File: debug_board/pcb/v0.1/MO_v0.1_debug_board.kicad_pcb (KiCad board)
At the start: 2 copper layers, 98.1 x 88 mm, 52 parts, among them j1 DAC_PWR, j10 nRF_PWR, j11 U0_TX, j12 nRF_VBUS, j13 SWDIO, j14 SWDCLK, j15 U0_RX, j16 nRF_DCCH, j2 SD_nFLAG, j3 DAC_nFLAG, j4 nRF_RESET, j5 FW_PWR_FAULT, j6 SD_PWR, j7 3v3_PI, j8 3v3_LDO, j9 GND

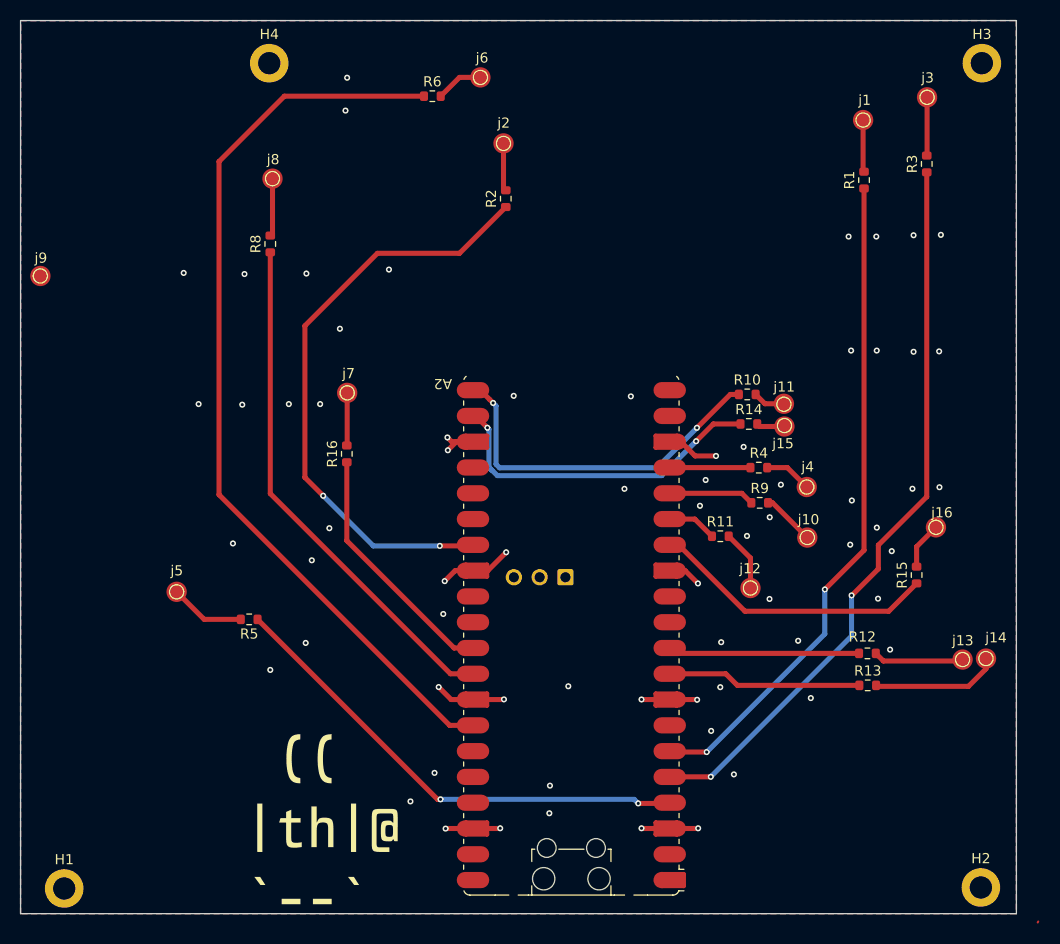
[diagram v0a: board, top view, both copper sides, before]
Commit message: Update debug board to use pi zero instead of pico
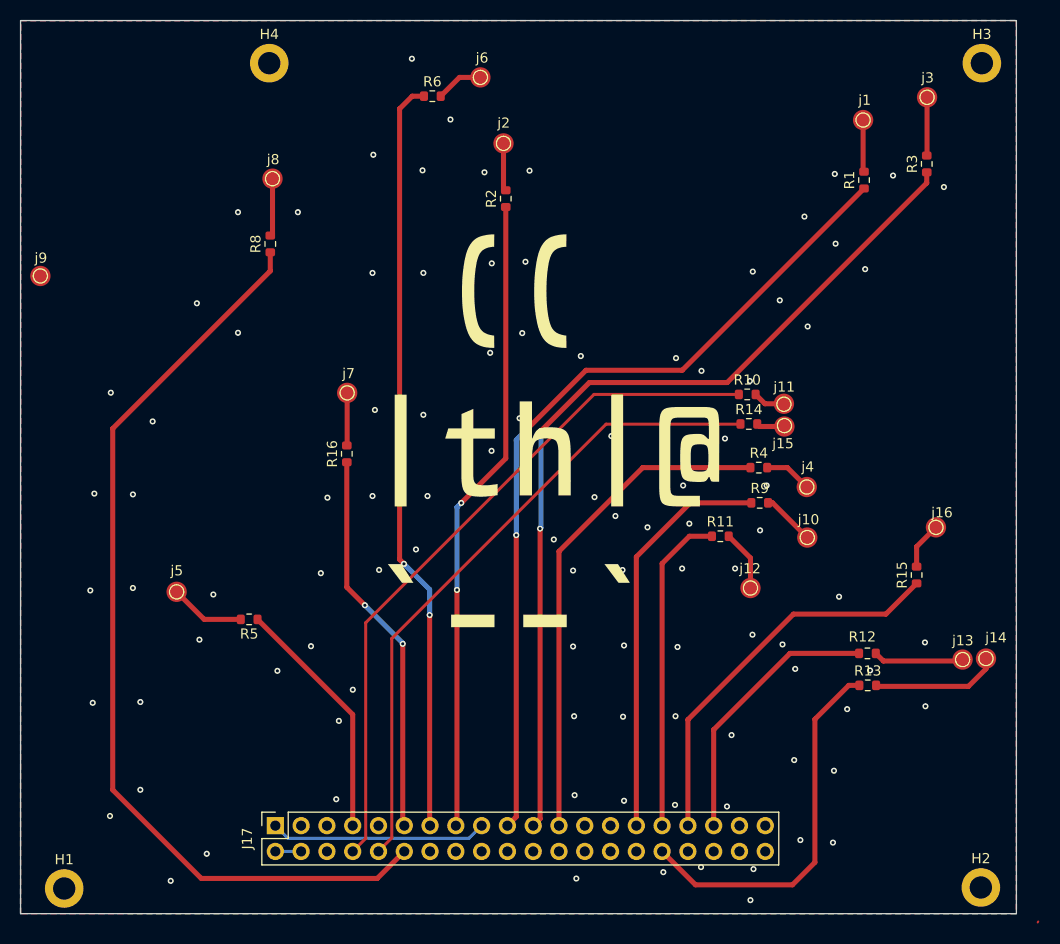
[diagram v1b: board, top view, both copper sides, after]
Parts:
- removed A2: RaspberryPi_Pico_W, Module:RaspberryPi_Pico_W_SMD_HandSolder
- added J17: Raspberry_Pi_4, Connector_PinSocket_2.54mm:PinSocket_2x20_P2.54mm_Vertical, F.Cu at (161.2, 109.6)
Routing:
- net GND: track 44.6 -> 0.00 mm, vias 68 -> 101
- net /3v3_LDO: track 51.1 -> 92.8 mm
- net /nRF_RESET: track 7.95 -> 49.3 mm
- net /U0_TX: track 35.7 -> 69.1 mm, vias 2 -> 0
- net /nRF_PWR: track 8.43 -> 40.0 mm
- net /U0_RX: track 33.4 -> 64.6 mm, vias 2 -> 0
- net /nRF_VBUS: track 4.86 -> 31.8 mm
- net /FW_PWR_FAULT: track 48.1 -> 24.2 mm, vias 2 -> 0
- net Net-(J17-3V3-Pad1): track 0.00 -> 21.3 mm
- net /SWDCLK: track 19.2 -> 37.2 mm
- net /DAC_PWR: track 65.6 -> 82.9 mm
- net /DAC_nFLAG: track 72.4 -> 88.4 mm
- net /SD_PWR: track 90.1 -> 74.8 mm, vias 0 -> 2
- net /3v3_PI: track 24.5 -> 38.1 mm, vias 0 -> 2
- net /nRF_DCCH: track 28.2 -> 38.5 mm
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
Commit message: Clean up silkscreen and fab files for debug board
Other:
- board text added: "TH-1-MO Debug board Rev: 1 31/08/2026 For MO rev: 0 (devkit)"
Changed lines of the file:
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@@
 		(capping no)
 		(filling no)
-		(zone_defaults)
+		(aux_axis_origin 136.08 118.27)
+		(grid_origin 136.08 118.27)
 		(pcbplotparams
 			(layerselection 0x00000000_00000000_55555555_5755f5ff)
@@
 			(usegerberattributes yes)
 			(usegerberadvancedattributes yes)
-			(creategerberjobfile yes)
+			(creategerberjobfile no)
 			(dashed_line_dash_ratio 12)
 			(dashed_line_gap_ratio 3)
@@
 			(plotframeref no)
 			(mode 1)
-			(useauxorigin no)
+			(useauxorigin yes)
 			(pdf_front_fp_property_popups yes)
 			(pdf_back_fp_property_popups yes)
@@
 			(plotpadnumbers no)
 			(hidednponfab no)
-			(sketchdnponfab yes)
-			(crossoutdnponfab yes)
+			(sketchdnponfab no)
+			(crossoutdnponfab no)
 			(subtractmaskfromsilk no)
 			(outputformat 1)
 			(mirror no)
-			(drillshape 1)
+			(drillshape 0)
 			(scaleselection 1)
-			(outputdirectory "")
+			(outputdirectory "fabrication/")
 		)
 	)
@@
 		(layer "Edge.Cuts")
 	)
+	(gr_text "TH-1-MO Debug board\nRev: 1\n31/08/2026\nFor MO rev: 0 (devkit)"
+		(at 188.79 41.75 0)
+		(layer "F.SilkS")
+		(effects
+			(font
+				(size 1.5 1.5)
+				(thickness 0.3)
+				(bold yes)
+			)
+			(justify left bottom)
+		)
+	)
 	(gr_text "DIO"
 		(at 227.13 93.14 90)
@@
 	)
 	(segment
-		(start 219.17 46.83)
-		(end 201.26 64.74)
-		(width 0.5)
-		(layer "F.Cu")
-		(net "/DAC_PWR")
-	)
-	(segment
-		(start 184.91 80.98)
-		(end 184.91 108.73)
-		(width 0.5)
-		(layer "F.Cu")
-		(net "/DAC_PWR")
-	)
-	(segment
-		(start 191.78 64.74)
-		(end 185.96 70.56)
-		(width 0.5)
-		(layer "F.Cu")
-		(net "/DAC_PWR")
-	)
-	(segment
-		(start 184.91 108.73)
-		(end 184.04 109.6)
+		(start 211.62 74.33)
+		(end 213.53 76.24)
 		(width 0.5)
 		(layer "F.Cu")
-		(net "/DAC_PWR")
+		(net "Net-(R4-Pad2)")
 	)
 	(segment
-		(start 201.26 64.74)
-		(end 191.78 64.74)
+		(start 209.63 74.33)
+		(end 211.62 74.33)
 		(width 0.5)
 		(layer "F.Cu")
-		(net "/DAC_PWR")
-	)
-	(via
-		(at 184.91 80.98)
-		(size 0.6)
-		(drill 0.3)
-		(layers "F.Cu" "B.Cu")
-		(net "/DAC_PWR")
-	)
-	(via
-		(at 185.96 70.56)
-		(size 0.6)
-		(drill 0.3)
-		(layers "F.Cu" "B.Cu")
-		(net "/DAC_PWR")
+		(net "Net-(R4-Pad2)")
 	)
 	(segment
-		(start 184.91 71.61)
-		(end 184.91 80.98)
-		(width 0.5)
+		(start 161.18 109.6)
+		(end 162.42 110.84)
+		(width 0.3)
 		(layer "B.Cu")
-		(net "/DAC_PWR")
+		(net "Net-(J17-3V3-Pad1)")
 	)
 	(segment
-		(start 185.96 70.56)
-		(end 184.91 71.61)
-		(width 0.5)
+		(start 180.26 110.84)
+		(end 181.5 109.6)
+		(width 0.3)
 		(layer "B.Cu")
-		(net "/DAC_PWR")
-	)
-	(segment
-		(start 204.36 100.15)
-		(end 204.36 109.6)
-		(width 0.5)
-		(layer "F.Cu")
-		(net "/SWDIO")
-	)
-	(segment
-		(start 218.68 92.63)
-		(end 211.88 92.63)
-		(width 0.5)
-		(layer "F.Cu")
-		(net "/SWDIO")
-	)
-	(segment
-		(start 211.88 92.63)
-		(end 204.36 100.15)
-		(width 0.5)
-		(layer "F.Cu")
-		(net "/SWDIO")
-	)
-	(segment
-		(start 212.22 88.76)
-		(end 201.82 99.16)
-		(width 0.5)
-		(layer "F.Cu")
-		(net "/nRF_DCCH")
-	)
-	(segment
-		(start 201.82 99.16)
-		(end 201.82 109.6)
-		(width 0.5)
-		(layer "F.Cu")
-		(net "/nRF_DCCH")
-	)
-	(segment
-		(start 221.325 88.76)
-		(end 212.22 88.76)
-		(width 0.5)
-		(layer "F.Cu")
-		(net "/nRF_DCCH")
-	)
-	(segment
-		(start 224.35 85.735)
-		(end 221.325 88.76)
-		(width 0.5)
-		(layer "F.Cu")
-		(net "/nRF_DCCH")
-	)
-	(segment
-		(start 189.12 82.58)
-		(end 189.12 109.6)
-		(width 0.5)
-		(layer "F.Cu")
-		(net "/nRF_RESET")
+		(net "Net-(J17-3V3-Pad1)")
 	)
 	(segment
-		(start 207.98 74.33)
-		(end 197.37 74.33)
-		(width 0.5)
-		(layer "F.Cu")
-		(net "/nRF_RESET")
+		(start 162.42 110.84)
+		(end 180.26 110.84)
+		(width 0.3)
+		(layer "B.Cu")
+		(net "Net-(J17-3V3-Pad1)")
 	)
 	(segment
-		(start 197.37 74.33)
-		(end 189.12 82.58)
-		(width 0.5)
-		(layer "F.Cu")
-		(net "/nRF_RESET")
+		(start 163.72 112.14)
+		(end 161.18 112.14)
+		(width 0.3)
+		(layer "B.Cu")
+		(net "Net-(J17-5V-Pad2)")
 	)
 	(segment
@@
 	)
 	(segment
-		(start 211.62 74.33)
-		(end 213.53 76.24)
+		(start 219.17 46.83)
+		(end 201.26 64.74)
 		(width 0.5)
 		(layer "F.Cu")
-		(net "Net-(R4-Pad2)")
+		(net "/DAC_PWR")
 	)
 	(segment
-		(start 209.63 74.33)
-		(end 211.62 74.33)
+		(start 184.91 80.98)
+		(end 184.91 108.73)
 		(width 0.5)
 		(layer "F.Cu")
-		(net "Net-(R4-Pad2)")
+		(net "/DAC_PWR")
+	)
+	(segment
+		(start 191.78 64.74)
+		(end 185.96 70.56)
+		(width 0.5)
+		(layer "F.Cu")
+		(net "/DAC_PWR")
+	)
+	(segment
+		(start 184.91 108.73)
+		(end 184.04 109.6)
+		(width 0.5)
+		(layer "F.Cu")
+		(net "/DAC_PWR")
+	)
+	(segment
+		(start 201.26 64.74)
+		(end 191.78 64.74)
+		(width 0.5)
+		(layer "F.Cu")
+		(net "/DAC_PWR")
+	)
+	(via
+		(at 184.91 80.98)
+		(size 0.6)
+		(drill 0.3)
+		(layers "F.Cu" "B.Cu")
+		(net "/DAC_PWR")
+	)
+	(via
+		(at 185.96 70.56)
+		(size 0.6)
+		(drill 0.3)
+		(layers "F.Cu" "B.Cu")
+		(net "/DAC_PWR")
+	)
+	(segment
+		(start 184.91 71.61)
+		(end 184.91 80.98)
+		(width 0.5)
+		(layer "B.Cu")
+		(net "/DAC_PWR")
+	)
+	(segment
+		(start 185.96 70.56)
+		(end 184.91 71.61)
+		(width 0.5)
+		(layer "B.Cu")
+		(net "/DAC_PWR")
+	)
+	(segment
+		(start 189.12 82.58)
+		(end 189.12 109.6)
+		(width 0.5)
+		(layer "F.Cu")
+		(net "/nRF_RESET")
+	)
+	(segment
+		(start 207.98 74.33)
+		(end 197.37 74.33)
+		(width 0.5)
+		(layer "F.Cu")
+		(net "/nRF_RESET")
+	)
+	(segment
+		(start 197.37 74.33)
+		(end 189.12 82.58)
+		(width 0.5)
+		(layer "F.Cu")
+		(net "/nRF_RESET")
+	)
+	(segment
+		(start 212.22 88.76)
+		(end 201.82 99.16)
+		(width 0.5)
+		(layer "F.Cu")
+		(net "/nRF_DCCH")
+	)
+	(segment
+		(start 201.82 99.16)
+		(end 201.82 109.6)
+		(width 0.5)
+		(layer "F.Cu")
+		(net "/nRF_DCCH")
+	)
+	(segment
+		(start 221.325 88.76)
+		(end 212.22 88.76)
+		(width 0.5)
+		(layer "F.Cu")
+		(net "/nRF_DCCH")
+	)
+	(segment
+		(start 224.35 85.735)
+		(end 221.325 88.76)
+		(width 0.5)
+		(layer "F.Cu")
+		(net "/nRF_DCCH")
+	)
+	(segment
+		(start 204.36 100.15)
+		(end 204.36 109.6)
+		(width 0.5)
+		(layer "F.Cu")
+		(net "/SWDIO")
+	)
+	(segment
+		(start 218.68 92.63)
+		(end 211.88 92.63)
+		(width 0.5)
+		(layer "F.Cu")
+		(net "/SWDIO")
+	)
+	(segment
+		(start 211.88 92.63)
+		(end 204.36 100.15)
+		(width 0.5)
+		(layer "F.Cu")
+		(net "/SWDIO")
 	)
 	(segment
@@
 		(net "Net-(R6-Pad2)")
 	)
-	(segment
-		(start 161.18 109.6)
-		(end 162.42 110.84)
-		(width 0.3)
-		(layer "B.Cu")
-		(net "Net-(J17-3V3-Pad1)")
-	)
-	(segment
-		(start 180.26 110.84)
-		(end 181.5 109.6)
-		(width 0.3)
-		(layer "B.Cu")
-		(net "Net-(J17-3V3-Pad1)")
-	)
-	(segment
-		(start 162.42 110.84)
-		(end 180.26 110.84)
-		(width 0.3)
-		(layer "B.Cu")
-		(net "Net-(J17-3V3-Pad1)")
-	)
-	(segment
-		(start 163.72 112.14)
-		(end 161.18 112.14)
-		(width 0.3)
-		(layer "B.Cu")
-		(net "Net-(J17-5V-Pad2)")
-	)
 	(zone
